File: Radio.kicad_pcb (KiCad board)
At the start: 2 copper layers, 12 parts, among them U1 RDA5807M_Module, U2 LM386

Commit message: Add files via upload
updated schematic and board design with traces for Radio and Amplifier. V2
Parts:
- removed U2: LM386, Package_TO_SOT_SMD:HVSOF6
- added U3: LM386N-4_NOPB, LM386:DIP08, F.Cu at (99.0, 63.0)
- A1: footprint Module:RaspberryPi_Pico_W_SMD_HandSolder -> ECE 299:RPi_Pico_TH
- LS1: footprint Buzzer_Beeper:Speaker_CUI_CMR-1206S-67 -> ECE 299:CUE_CMA-4544PF-W
- RV1: footprint Resistor_SMD:R_0201_0603Metric_Pad0.64x0.40mm_HandSolder -> Potentiometer_THT:Potentiometer_ACP_CA9-V10_Vertical
- U1: footprint ECE 299:RDA5807M_Module_SM -> ECE 299:RDA5807M_Module_TH; moved to B.Cu
- moved U1 80.5 mm to (156.0, 55.0)
- moved A1 70.7 mm to (127.0, 62.0)
- moved R2 67.8 mm to (141.4, 57.0), turned to 180 degrees
- moved R1 63.7 mm to (141.4, 61.3), turned to 180 degrees
- moved LS1 46.2 mm to (145.0, 76.0), turned to 90 degrees
- moved RV1 42.9 mm to (112.0, 45.5), turned to 180 degrees
- moved Bypass1 33.5 mm to (111.6, 81.0)
- moved R3 15.9 mm to (103.0, 81.0)
- moved C1 12.9 mm to (105.6, 72.0)
- moved C2 11.3 mm to (111.4, 63.0)
- moved C3 3.00 mm to (109.6, 72.0)
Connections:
- Bypass1 pad 1: GND -> Net-(Bypass1-Pad1)
- Bypass1 pad 2: Net-(U2-BYPASS) -> GND
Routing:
- net +3V3: track 0.00 -> 68.2 mm
- net GND: track 0.00 -> 66.8 mm
- net Net-(U1-LOUT): track 0.00 -> 55.6 mm
- net Net-(C3-Pad2): track 0.00 -> 38.1 mm
- net Net-(Bypass1-Pad1): track 0.00 -> 29.9 mm
- net Net-(A1-GPIO26_ADC0): track 0.00 -> 13.0 mm
- net Net-(RV1-Pad2): track 0.00 -> 13.0 mm
- net Net-(A1-GPIO27_ADC1): track 0.00 -> 12.8 mm
- net Net-(C1-Pad1): track 0.00 -> 12.0 mm
- net Net-(C2-Pad2): track 0.00 -> 10.8 mm
- net Net-(C1-Pad2): track 0.00 -> 10.1 mm
- net Net-(C2-Pad1): track 0.00 -> 9.77 mm
- added copper zone on B.Cu, net GND

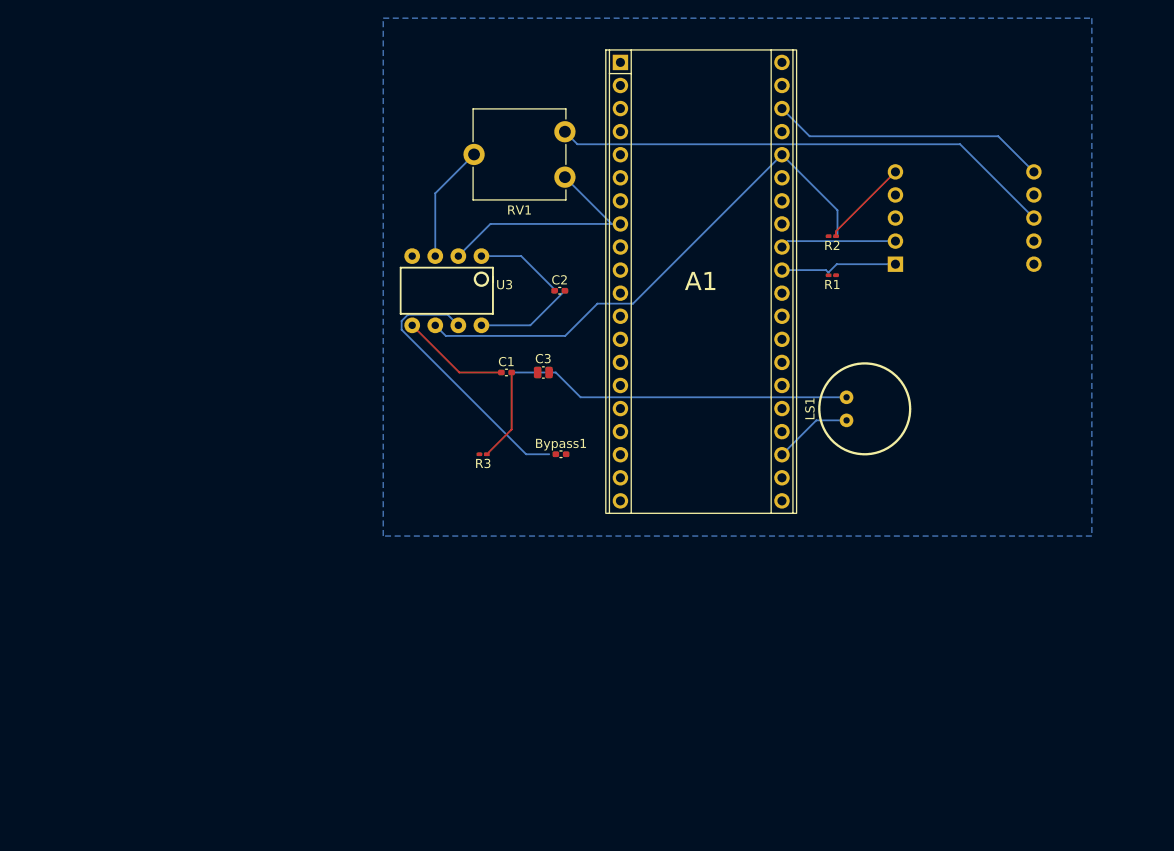
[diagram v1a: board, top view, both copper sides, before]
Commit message: Add files via upload
Initial PCB design for the clock-radio, subject to alterations and changes including;

- Traces
- Spacing
- Footprint alterations and port connections
- Mounting Hole Spacing + Size
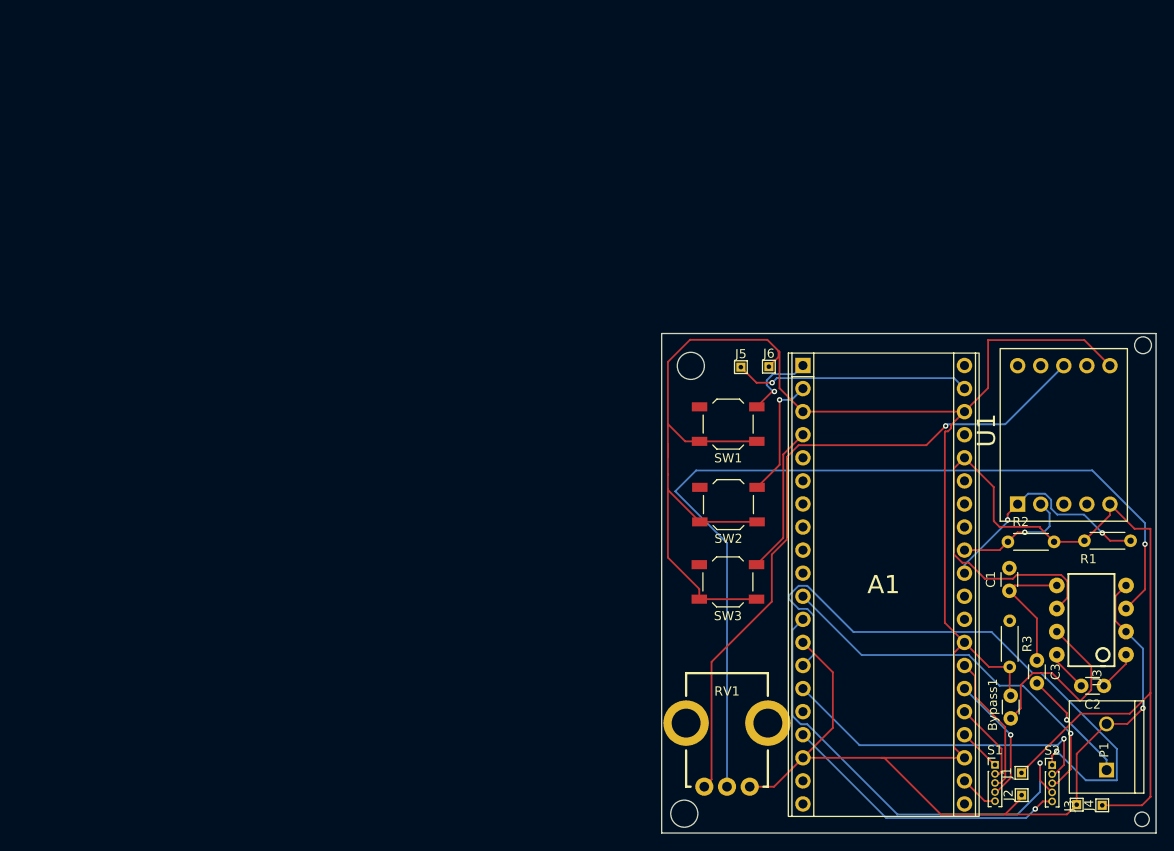
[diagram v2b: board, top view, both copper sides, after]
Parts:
- removed LS1: Speaker, ECE 299:CUE_CMA-4544PF-W
- added J1: 3V3_PIN, TestPoint:TestPoint_THTPad_1.0x1.0mm_Drill0.5mm, F.Cu at (162.2, 116.1)
- added J2: GND_PIN, TestPoint:TestPoint_THTPad_1.0x1.0mm_Drill0.5mm, F.Cu at (162.3, 118.5)
- added J3: GND_PIN, TestPoint:TestPoint_THTPad_1.0x1.0mm_Drill0.5mm, F.Cu at (168.3, 119.6)
- added J4: 3V3_PIN, TestPoint:TestPoint_THTPad_1.0x1.0mm_Drill0.5mm, F.Cu at (171.1, 119.6)
- added J5: 5V5_INPUT_PIN, TestPoint:TestPoint_THTPad_1.0x1.0mm_Drill0.5mm, F.Cu at (131.4, 71.4)
- added J6: Voltage_GND, TestPoint:TestPoint_THTPad_1.0x1.0mm_Drill0.5mm, F.Cu at (134.4, 71.4)
- added P1: Speaker_Connect, 2_pin:TE_282837-2, F.Cu at (171.6, 113.2)
- added S1: OLED_HOUR, Connector_PinHeader_1.00mm:PinHeader_1x05_P1.00mm_Vertical, F.Cu at (159.3, 115.2)
- added S2: OLED_MIN, Connector_PinHeader_1.00mm:PinHeader_1x05_P1.00mm_Vertical, F.Cu at (165.6, 115.2)
- added SW1: SW_Push, Button_Switch_SMD:SW_SPST_TL3342, F.Cu at (130.0, 77.7)
- added SW2: SW_Push, Button_Switch_SMD:SW_SPST_TL3342, F.Cu at (130.0, 86.5)
- added SW3: SW_Push, Button_Switch_SMD:SW_SPST_TL3342, F.Cu at (129.9, 95.0)
- Bypass1, C1, C2: footprint Capacitor_SMD:C_0402_1005Metric_Pad0.74x0.62mm_HandSolder -> Capacitor_THT:C_Disc_D3.0mm_W1.6mm_P2.50mm
- C3: footprint Capacitor_SMD:C_0504_1310Metric_Pad0.83x1.28mm_HandSolder -> Capacitor_THT:C_Disc_D3.0mm_W1.6mm_P2.50mm
- R1, R2, R3: footprint Resistor_SMD:R_0201_0603Metric_Pad0.64x0.40mm_HandSolder -> Resistor_THT:R_Axial_DIN0204_L3.6mm_D1.6mm_P5.08mm_Horizontal
- RV1: footprint Potentiometer_THT:Potentiometer_ACP_CA9-V10_Vertical -> ECE 299:Bourns_PTV09_Horiz
- U1: moved to F.Cu
- moved U3 79.7 mm to (169.9, 99.2), turned to 90 degrees
- moved RV1 74.3 mm to (129.8, 117.6), turned to 0 degrees
- moved C2 74.0 mm to (171.3, 106.5), turned to 180 degrees
- moved C3 62.9 mm to (163.9, 103.7), turned to -90 degrees
- moved R3 60.8 mm to (161.0, 99.3), turned to -90 degrees
- moved C1 60.3 mm to (160.9, 96.0), turned to 90 degrees
- moved Bypass1 57.4 mm to (161.1, 110.1), turned to 90 degrees
- moved R2 41.6 mm to (165.8, 90.6)
- moved R1 40.3 mm to (169.2, 90.5), turned to 0 degrees
- moved A1 38.9 mm to (147.1, 95.4)
- moved U1 26.2 mm to (166.9, 78.9), turned to 90 degrees
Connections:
- A1 pad 1: unconnected-(A1-GPIO0-Pad1) -> Net-(A1-GPIO0)
- A1 pad 11: unconnected-(A1-GPIO8-Pad11) -> Net-(A1-GPIO8)
- A1 pad 12: unconnected-(A1-GPIO9-Pad12) -> Net-(A1-GPIO9)
- A1 pad 14: unconnected-(A1-GPIO10-Pad14) -> Net-(A1-GPIO10)
- A1 pad 15: unconnected-(A1-GPIO11-Pad15) -> Net-(A1-GPIO11)
- A1 pad 17: unconnected-(A1-GPIO13-Pad17) -> Net-(A1-GPIO13)
- A1 pad 2: unconnected-(A1-GPIO1-Pad2) -> Net-(A1-GPIO1)
- A1 pad 22: unconnected-(A1-GPIO17-Pad22) -> Net-(A1-GPIO17)
- A1 pad 24: unconnected-(A1-GPIO18-Pad24) -> Net-(A1-GPIO18)
- A1 pad 25: unconnected-(A1-GPIO19-Pad25) -> Net-(A1-GPIO19)
- A1 pad 26: unconnected-(A1-GPIO20-Pad26) -> Net-(A1-GPIO20)
- A1 pad 27: unconnected-(A1-GPIO21-Pad27) -> Net-(A1-GPIO21)
- A1 pad 39: unconnected-(A1-VSYS-Pad39) -> Net-(A1-VSYS)
- A1 pad 4: unconnected-(A1-GPIO2-Pad4) -> Net-(A1-GPIO2)
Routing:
- net GND: track 66.8 -> 270.6 mm, vias 0 -> 1
- net Net-(RV1-Pad2): track 13.0 -> 100.2 mm, vias 0 -> 1
- net Net-(A1-GPIO10): track 0.00 -> 67.0 mm, vias 0 -> 1
- net Net-(A1-GPIO9): track 0.00 -> 50.9 mm, vias 0 -> 1
- net +3V3: track 68.2 -> 111.8 mm
- net Net-(A1-GPIO8): track 0.00 -> 42.3 mm, vias 0 -> 1
- net Net-(A1-GPIO11): track 0.00 -> 36.2 mm, vias 0 -> 1
- net Net-(A1-GPIO13): track 0.00 -> 32.0 mm, vias 0 -> 1
- net Net-(A1-VSYS): track 0.00 -> 26.0 mm, vias 0 -> 1
- net Net-(C3-Pad2): track 38.1 -> 12.7 mm, vias 0 -> 1
- net Net-(U1-LOUT): track 55.6 -> 74.7 mm, vias 0 -> 1
- net Net-(A1-GPIO2): track 0.00 -> 16.4 mm
- net Net-(A1-GPIO21): track 0.00 -> 15.6 mm
- net Net-(A1-GPIO20): track 0.00 -> 14.3 mm, vias 0 -> 1
- net Net-(A1-GPIO1): track 0.00 -> 13.7 mm, vias 0 -> 1
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- removed copper zone on B.Cu, net GND
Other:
- board outline added: 54.4 x 55 mm
